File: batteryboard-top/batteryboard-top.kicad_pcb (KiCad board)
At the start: 2 copper layers, 46.8 x 46.8 mm, 7 parts, among them J1 Conn 02x10 1.27mm, J2 Conn_01x02, J3 Conn_01x02

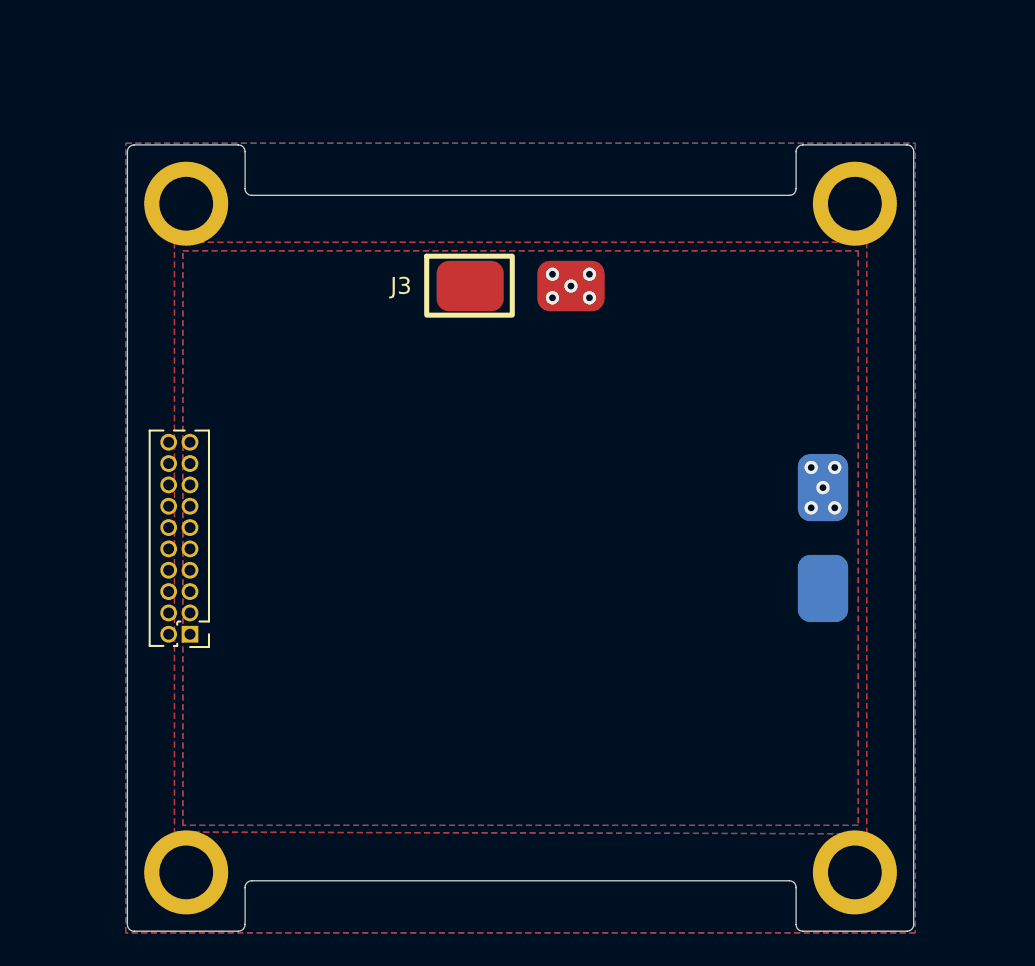
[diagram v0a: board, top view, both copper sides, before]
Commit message: Added connectors and traces
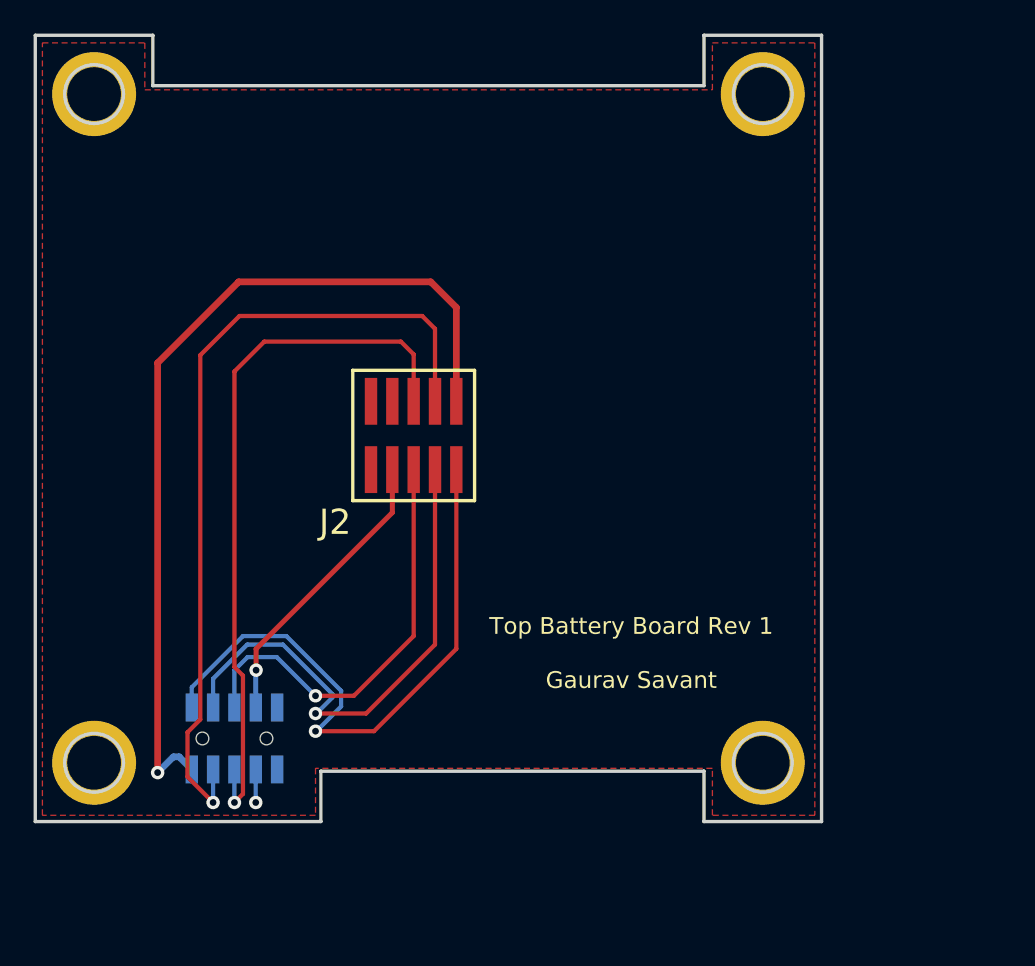
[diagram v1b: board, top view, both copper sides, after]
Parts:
- removed J3: Conn_01x02, batteryboard:Battery Pads
- J1: value Conn 02x10 1.27mm -> Conn_02x05_Odd_Even; footprint Connector_PinHeader_1.27mm:PinHeader_2x10_P1.27mm_Vertical -> batteryboard:SAMTEC_FLE-105-01-G-DV-A; moved to B.Cu
- J2: value Conn_01x02 -> Conn_02x05_Odd_Even; footprint batteryboard:Battery Pads -> batteryboard:SAMTEC-FTS-105-01-X-DV; moved to F.Cu
- moved J2 25.1 mm to (138.9, 91.7), turned to 0 degrees
- moved H1 8.52 mm to (119.9, 71.4)
- moved H2 8.52 mm to (159.7, 71.4)
- moved H4 8.52 mm to (119.9, 111.2)
- moved H3 8.52 mm to (159.7, 111.2)
- moved J1 6.74 mm to (128.3, 109.7)
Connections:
- J1 pad 10: unconnected-(J1-Pad10) -> VBUS
- J2 pad 1: BATT_P_SW -> unconnected-(J2-Pad1)
- J2 pad 2: BATT_N_SW -> unconnected-(J2-Pad2)
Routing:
- net VBUS: track 0.00 -> 53.1 mm, vias 0 -> 1
- net COIL_N: track 0.00 -> 50.4 mm, vias 0 -> 1
- net SCL3: track 0.00 -> 42.6 mm, vias 0 -> 1
- net BATT_P: track 0.00 -> 36.9 mm, vias 0 -> 1
- net COIL_P: track 0.00 -> 31.7 mm, vias 0 -> 1
- net SDA3: track 0.00 -> 25.5 mm, vias 0 -> 1
- net +3V3: track 0.00 -> 17.5 mm, vias 0 -> 1
- net GND: track 0.00 -> 1.97 mm, vias 0 -> 1
- net BATT_P_SW: vias 5 -> 0
- net BATT_N_SW: vias 5 -> 0
- removed copper zone on B.Cu, net BATT_N_SW
- removed copper zone on F.Cu, net BATT_P_SW
- removed copper zone on B.Cu, net GND
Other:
- outline, holes or cut-outs redrawn
- board text added: "Top Battery Board Rev 1 Gaurav Savant"

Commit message: Added proper connectors and added traces
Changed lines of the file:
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@@
     (property "Sheetname" "")
     (attr through_hole)
-    (fp_text reference "J1" (at -1 4.33) (layer "B.SilkS")
+    (fp_text reference "J1" (at 0 4.064) (layer "B.SilkS")
       (effects (font (size 1 1) (thickness 0.15)) (justify mirror))
     )
@@
   (via (at 129.54 113.538) (size 0.8) (drill 0.4) (layers "F.Cu" "B.Cu") (free) (net 1))
   (segment (start 129.54 111.5705) (end 129.54 113.538) (width 0.254) (layer "B.Cu") (net 1))
-  (segment (start 141.478 84.074) (end 141.478 89.662) (width 0.4) (layer "F.Cu") (net 2))
-  (segment (start 139.954 82.55) (end 141.478 84.074) (width 0.4) (layer "F.Cu") (net 2))
-  (segment (start 123.698 111.76) (end 123.698 87.376) (width 0.4) (layer "F.Cu") (net 2))
-  (segment (start 123.698 87.376) (end 128.524 82.55) (width 0.4) (layer "F.Cu") (net 2))
-  (segment (start 128.524 82.55) (end 139.954 82.55) (width 0.4) (layer "F.Cu") (net 2))
+  (segment (start 141.478 84.074) (end 141.478 89.662) (width 0.762) (layer "F.Cu") (net 2))
+  (segment (start 139.954 82.55) (end 141.478 84.074) (width 0.762) (layer "F.Cu") (net 2))
+  (segment (start 123.698 111.76) (end 123.698 87.376) (width 0.762) (layer "F.Cu") (net 2))
+  (segment (start 123.698 87.376) (end 128.524 82.55) (width 0.762) (layer "F.Cu") (net 2))
+  (segment (start 128.524 82.55) (end 139.954 82.55) (width 0.762) (layer "F.Cu") (net 2))
   (via (at 123.698 111.76) (size 0.8) (drill 0.4) (layers "F.Cu" "B.Cu") (free) (net 2))
-  (segment (start 123.698 111.76) (end 124.638011 110.819989) (width 0.4) (layer "B.Cu") (net 2))
-  (segment (start 124.979489 110.819989) (end 125.73 111.5705) (width 0.4) (layer "B.Cu") (net 2))
-  (segment (start 124.638011 110.819989) (end 124.979489 110.819989) (width 0.4) (layer "B.Cu") (net 2))
-  (segment (start 129.5585 104.394) (end 137.668 96.2845) (width 0.3) (layer "F.Cu") (net 5))
-  (segment (start 137.668 96.2845) (end 137.668 93.726) (width 0.3) (layer "F.Cu") (net 5))
-  (segment (start 129.5585 105.664) (end 129.5585 104.394) (width 0.3) (layer "F.Cu") (net 5))
+  (segment (start 123.698 111.76) (end 124.638011 110.819989) (width 0.762) (layer "B.Cu") (net 2))
+  (segment (start 124.979489 110.819989) (end 125.73 111.5705) (width 0.762) (layer "B.Cu") (net 2))
+  (segment (start 124.638011 110.819989) (end 124.979489 110.819989) (width 0.762) (layer "B.Cu") (net 2))
+  (segment (start 129.5585 104.394) (end 137.668 96.2845) (width 0.5) (layer "F.Cu") (net 5))
+  (segment (start 137.668 96.2845) (end 137.668 93.726) (width 0.5) (layer "F.Cu") (net 5))
+  (segment (start 129.5585 105.664) (end 129.5585 104.394) (width 0.5) (layer "F.Cu") (net 5))
   (via (at 129.5585 105.664) (size 0.8) (drill 0.4) (layers "F.Cu" "B.Cu") (free) (net 5))
   (segment (start 129.54 105.6825) (end 129.5585 105.664) (width 0.254) (layer "B.Cu") (net 5))

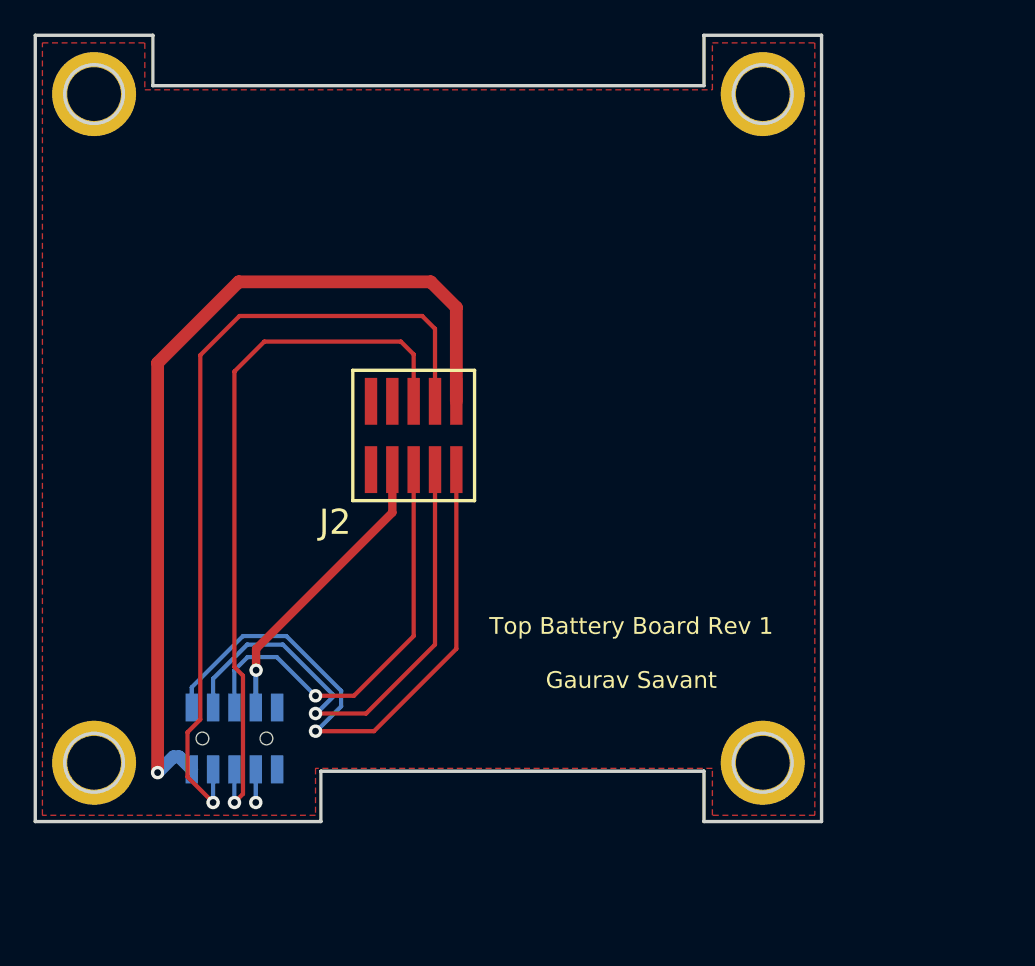
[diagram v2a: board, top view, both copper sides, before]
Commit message: Fixed design errors (some issues remain in middle) and fixed trace widths
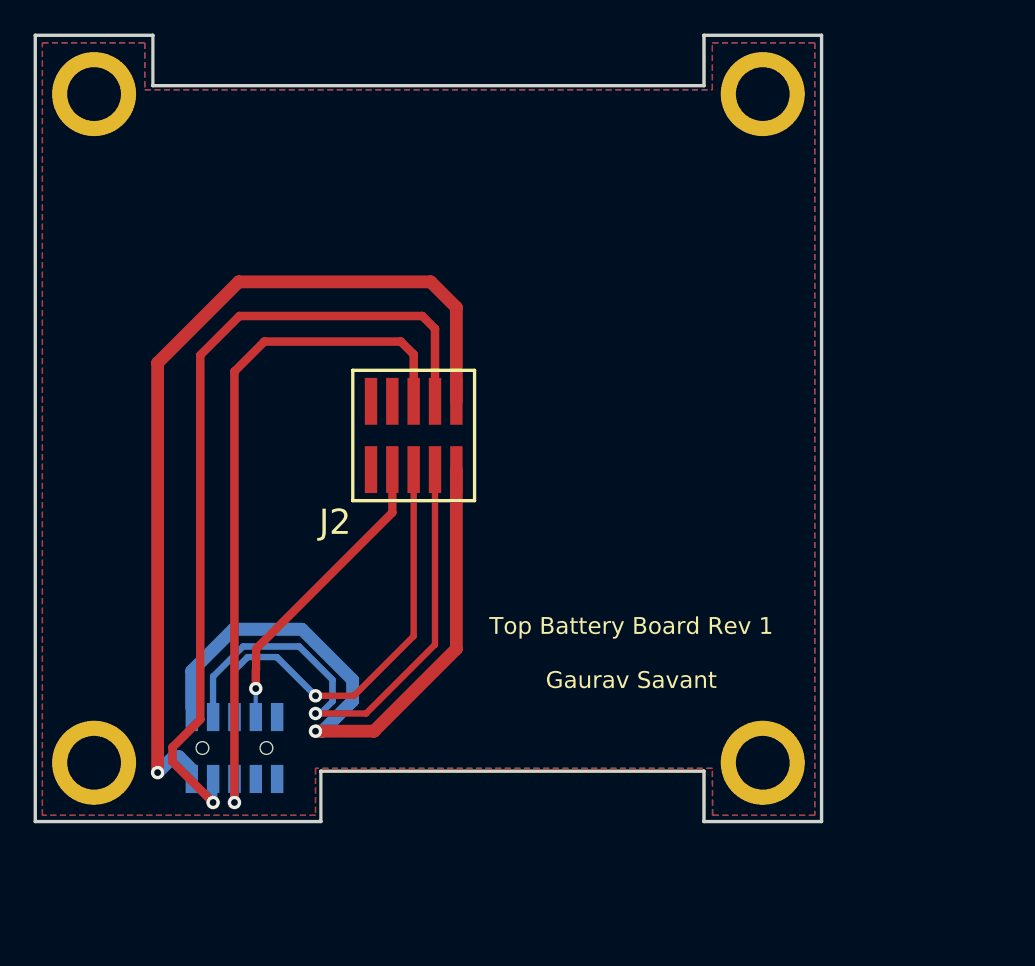
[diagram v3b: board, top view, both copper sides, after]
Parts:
- moved J1 0.57 mm to (128.3, 110.3)
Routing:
- net BATT_P: track 36.9 -> 39.3 mm
- net GND: track 1.97 -> 0.00 mm, vias 1 -> 0
- net COIL_P: track 31.7 -> 32.3 mm
- net +3V3: track 17.5 -> 18.1 mm
- net COIL_N: track 50.4 -> 49.8 mm
- added copper zone on B.Cu, net GND
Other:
- outline, holes or cut-outs redrawn

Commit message: Fixes and cleanup
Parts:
- added Ref**: Val**, custom-footprints:pycubed_mini_half, F.Cu at (151.3, 75.8)
- J2: footprint batteryboard:SAMTEC-FTS-105-01-X-DV -> batteryboard:FTS-105-XX-YY-DV-A
- moved H1 50.7 mm to (170.3, 76.6), turned to -90 degrees
- moved H2 46.3 mm to (170.3, 116.4), turned to -90 degrees
- moved H4 36.2 mm to (130.5, 76.6), turned to -90 degrees
- moved H3 29.7 mm to (130.5, 116.4), turned to -90 degrees
- moved J1 25.6 mm to (131.4, 84.9), turned to 90 degrees
- moved J2 11.7 mm to (150.0, 95.5), turned to 90 degrees
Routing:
- net VBUS: track 53.1 -> 25.4 mm
- net COIL_N: track 49.8 -> 25.9 mm
- net SCL3: track 42.1 -> 25.9 mm
- net +3V3: track 18.1 -> 26.9 mm
- net SDA3: track 25.5 -> 30.2 mm
- net BATT_P: track 39.3 -> 34.9 mm
- net COIL_P: track 32.3 -> 31.8 mm
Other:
- outline, holes or cut-outs redrawn
- board text added: "09-JUN-22"
- board text added: "v01"
